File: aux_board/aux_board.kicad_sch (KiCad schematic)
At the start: 20 parts, among them J1 Conn_02x13_Odd_Even, J2 Conn_02x03_Odd_Even, J3 Conn_02x04_Odd_Even, J4 Conn_01x02_Pin

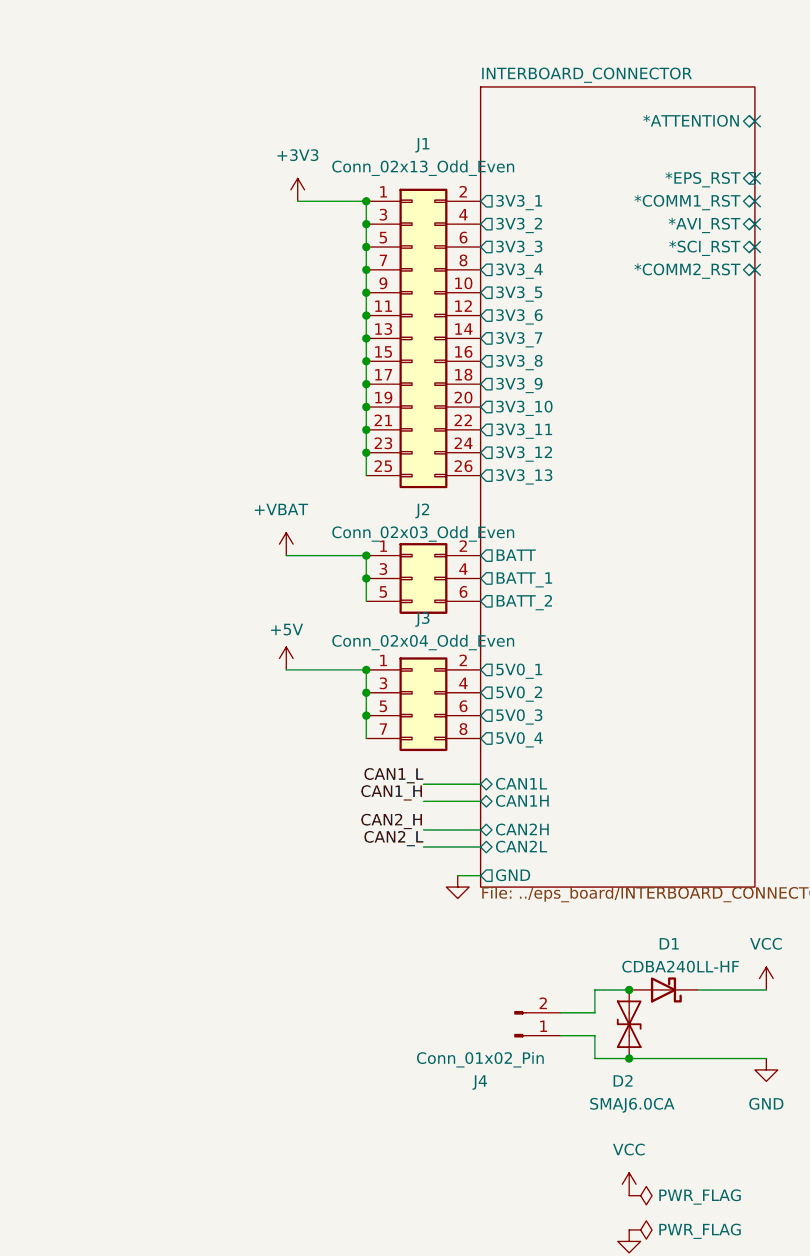
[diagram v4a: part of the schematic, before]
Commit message: assign can power to core powerm will need to use GPIO to enable power stndby from MCUs, finalize pc104 bus assignments
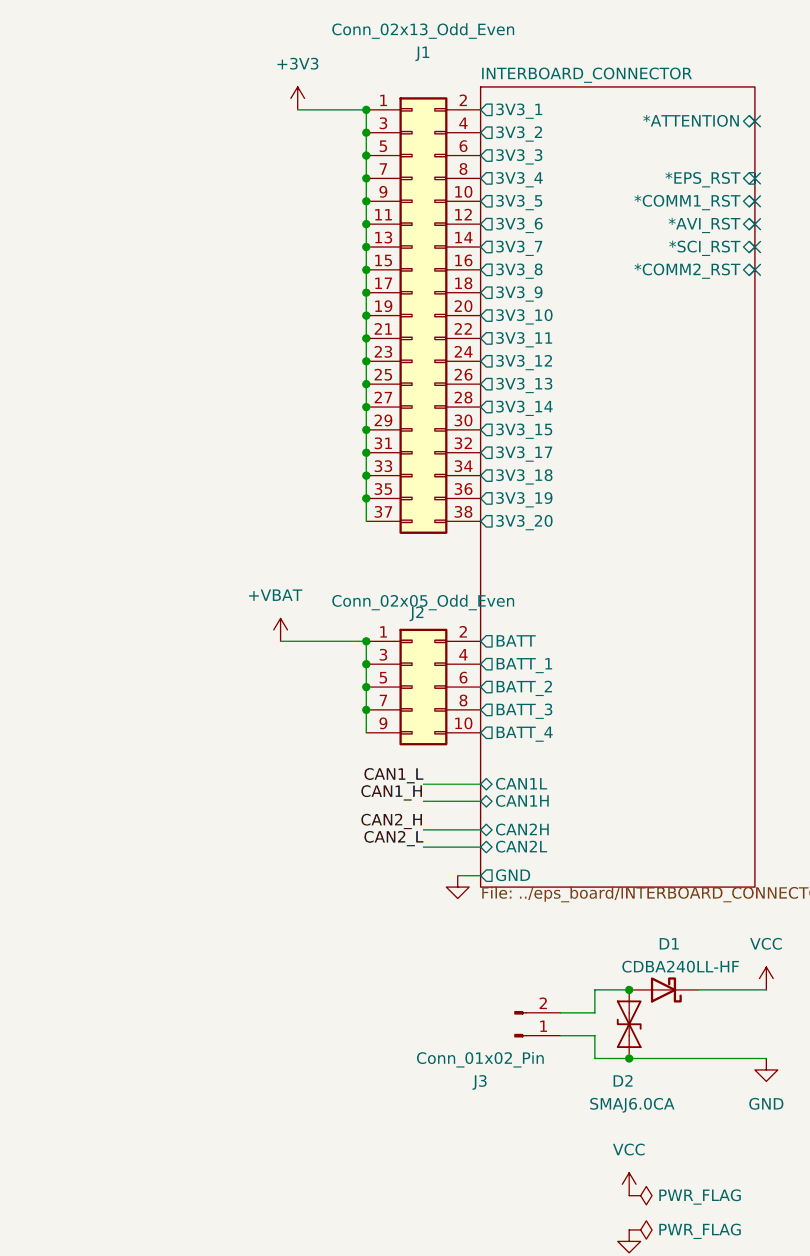
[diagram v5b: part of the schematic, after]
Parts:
- removed J1: Conn_02x13_Odd_Even, Connector_PinHeader_2.54mm:PinHeader_2x13_P2.54mm_Vertical, symbol Connector_Generic:Conn_02x13_Odd_Even
- removed J2: Conn_02x03_Odd_Even, Connector_PinHeader_2.54mm:PinHeader_2x03_P2.54mm_Vertical, symbol Connector_Generic:Conn_02x03_Odd_Even
- removed J3: Conn_02x04_Odd_Even, Connector_PinHeader_2.54mm:PinHeader_2x04_P2.54mm_Vertical, symbol Connector_Generic:Conn_02x04_Odd_Even
- added J1: Conn_02x13_Odd_Even, Connector_PinHeader_2.54mm:PinHeader_2x19_P2.54mm_Vertical, symbol Connector_Generic:Conn_02x19_Odd_Even
- added J2: Conn_02x05_Odd_Even, Connector_PinHeader_2.54mm:PinHeader_2x05_P2.54mm_Vertical, symbol Connector_Generic:Conn_02x05_Odd_Even
- renumbered J4 to J3
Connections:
- net +3V3: now also J1.1 (Pin_1), J1.11 (Pin_11), J1.13 (Pin_13), J1.15 (Pin_15), J1.17 (Pin_17), J1.19 (Pin_19), J1.21 (Pin_21), J1.23 (Pin_23), J1.25 (Pin_25), J1.27 (Pin_27), J1.29 (Pin_29), J1.3 (Pin_3), J1.31 (Pin_31), J1.33 (Pin_33), J1.35 (Pin_35), J1.37 (Pin_37), J1.5 (Pin_5), J1.7 (Pin_7), J1.9 (Pin_9)
- net +VBAT: now also J2.1 (Pin_1), J2.3 (Pin_3), J2.5 (Pin_5), J2.7 (Pin_7), J2.9 (Pin_9)
- net INTERBOARD_CONNECTOR/3V3_1: now also J1.2 (Pin_2)
- net INTERBOARD_CONNECTOR/3V3_10: now also J1.20 (Pin_20)
- net INTERBOARD_CONNECTOR/3V3_11: now also J1.22 (Pin_22)
- net INTERBOARD_CONNECTOR/3V3_12: now also J1.24 (Pin_24)
- net INTERBOARD_CONNECTOR/3V3_13: now also J1.26 (Pin_26)
- net INTERBOARD_CONNECTOR/3V3_2: now also J1.4 (Pin_4)
- net INTERBOARD_CONNECTOR/3V3_3: now also J1.6 (Pin_6)
- net INTERBOARD_CONNECTOR/3V3_4: now also J1.8 (Pin_8)
- net INTERBOARD_CONNECTOR/3V3_5: now also J1.10 (Pin_10)
- net INTERBOARD_CONNECTOR/3V3_6: now also J1.12 (Pin_12)
- net INTERBOARD_CONNECTOR/3V3_7: now also J1.14 (Pin_14)
- net INTERBOARD_CONNECTOR/3V3_8: now also J1.16 (Pin_16)
- net INTERBOARD_CONNECTOR/3V3_9: now also J1.18 (Pin_18)
- net INTERBOARD_CONNECTOR/BATT: now also J2.2 (Pin_2)
- net INTERBOARD_CONNECTOR/BATT_1: now also J2.4 (Pin_4)
- net INTERBOARD_CONNECTOR/BATT_2: now also J2.6 (Pin_6)
- new net INTERBOARD_CONNECTOR/3V3_14: J1.28 (Pin_28)
- new net INTERBOARD_CONNECTOR/3V3_15: J1.30 (Pin_30)
- new net INTERBOARD_CONNECTOR/3V3_17: J1.32 (Pin_32)
- new net INTERBOARD_CONNECTOR/3V3_18: J1.34 (Pin_34)
- new net INTERBOARD_CONNECTOR/3V3_19: J1.36 (Pin_36)
- new net INTERBOARD_CONNECTOR/3V3_20: J1.38 (Pin_38)
- new net INTERBOARD_CONNECTOR/BATT_3: J2.8 (Pin_8)
- new net INTERBOARD_CONNECTOR/BATT_4: J2.10 (Pin_10)
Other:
- sheet INTERBOARD_CONNECTOR ports: added 3V3_14, 3V3_15, 3V3_17, 3V3_18, 3V3_19, 3V3_20, BATT_3, BATT_4; removed 5V0_1, 5V0_2, 5V0_3, 5V0_4

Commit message: create and check BOM, check MC pinout, CAN standby and shutdown for each channel
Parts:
- D1, D3, D4, D5, D6: Amps (none) -> 2; Manufacturer (none) -> Comchip Technology; Part Number (none) -> CDBA240LL-HF; Voltage (none) -> 40
- D2: value SMAJ6.0CA -> SMAJ5.0A; Amps (none) -> 43.5; Manufacturer (none) -> SMC Diodes; Part Number (none) -> SMAJ5.0A; Voltage (none) -> 6
- H1, H2, H3, H4, J2, J3: now not fitted
- J1: value Conn_02x13_Odd_Even -> Conn_02x19_Odd_Even; now not fitted
- L1, L2, L3: value 1u -> 1uH; Amps (none) -> 3.2; Manufacturer (none) -> Murata; Part Number (none) -> DFE252012P-1R0M=P2
- R1: Manufacturer (none) -> YAGEO; Part Number (none) -> RT0603BRD07806KL; Tolerance (none) -> 0.1
- R2: value 673K4 -> 673K; Manufacturer (none) -> YAGEO; Part Number (none) -> RT0603BRD07673KL; Tolerance (none) -> 0.1
- R3: Manufacturer (none) -> YAGEO; Part Number (none) -> RT0603BRD07511KL; Tolerance (none) -> 0.1
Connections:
- no-connect marks 6 -> 0
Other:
- sheet CAN TO USB ports: added EXTI_0, EXTI_1, EXTI_2, EXTI_3, EXTI_4, EXTI_5; removed none

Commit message: reduce some R to 0402 for consistency with imported components
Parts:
- R1: footprint Resistor_SMD:R_0603_1608Metric_Pad0.98x0.95mm_HandSolder -> Resistor_SMD:R_0402_1005Metric_Pad0.72x0.64mm_HandSolder; Part Number RT0603BRD07806KL -> RT0402BRD07806KL
- R2: footprint Resistor_SMD:R_0603_1608Metric_Pad0.98x0.95mm_HandSolder -> Resistor_SMD:R_0402_1005Metric_Pad0.72x0.64mm_HandSolder; Part Number RT0603BRD07673KL -> RT0402BRD07673KL
- R3: footprint Resistor_SMD:R_0603_1608Metric_Pad0.98x0.95mm_HandSolder -> Resistor_SMD:R_0402_1005Metric_Pad0.72x0.64mm_HandSolder; Part Number RT0603BRD07511KL -> RT0402BRD07511KL
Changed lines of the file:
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@@
 			)
 		)
-		(property "Footprint" "Resistor_SMD:R_0603_1608Metric_Pad0.98x0.95mm_HandSolder"
+		(property "Footprint" "Resistor_SMD:R_0402_1005Metric_Pad0.72x0.64mm_HandSolder"
 			(at 103.505 81.788 90)
 			(effects
@@
 			)
 		)
-		(property "Part Number" "RT0603BRD07673KL"
+		(property "Part Number" "RT0402BRD07673KL"
 			(at 103.505 80.01 0)
 			(effects
@@
 			)
 		)
-		(property "Footprint" "Resistor_SMD:R_0603_1608Metric_Pad0.98x0.95mm_HandSolder"
+		(property "Footprint" "Resistor_SMD:R_0402_1005Metric_Pad0.72x0.64mm_HandSolder"
 			(at 103.505 105.283 90)
 			(effects
@@
 			)
 		)
-		(property "Part Number" "RT0603BRD07511KL"
+		(property "Part Number" "RT0402BRD07511KL"
 			(at 103.505 103.505 0)
 			(effects
@@
 			)
 		)
-		(property "Footprint" "Resistor_SMD:R_0603_1608Metric_Pad0.98x0.95mm_HandSolder"
+		(property "Footprint" "Resistor_SMD:R_0402_1005Metric_Pad0.72x0.64mm_HandSolder"
 			(at 103.505 57.023 90)
 			(effects
@@
 			)
 		)
-		(property "Part Number" "RT0603BRD07806KL"
+		(property "Part Number" "RT0402BRD07806KL"
 			(at 103.505 55.245 0)
 			(effects
